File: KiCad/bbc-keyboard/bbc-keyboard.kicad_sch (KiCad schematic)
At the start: 11 parts

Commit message: LEDs
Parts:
- LD1, LD2, LD3: footprint (none) -> LED_THT:LED_D5.0mm
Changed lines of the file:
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@@
       (effects (font (size 1.27 1.27)) (justify right))
     )
-    (property "Footprint" "" (id 2) (at 71.12 73.66 0)
+    (property "Footprint" "LED_THT:LED_D5.0mm" (id 2) (at 71.12 73.66 0)
       (effects (font (size 1.27 1.27)) hide)
     )
@@
       (effects (font (size 1.27 1.27)) (justify right))
     )
-    (property "Footprint" "" (id 2) (at 80.01 73.66 0)
+    (property "Footprint" "LED_THT:LED_D5.0mm" (id 2) (at 80.01 73.66 0)
       (effects (font (size 1.27 1.27)) hide)
     )
@@
       (effects (font (size 1.27 1.27)) (justify right))
     )
-    (property "Footprint" "" (id 2) (at 88.9 73.66 0)
+    (property "Footprint" "LED_THT:LED_D5.0mm" (id 2) (at 88.9 73.66 0)
       (effects (font (size 1.27 1.27)) hide)
     )
@@
     )
     (path "/5414043a-ed38-4cec-828b-be5302069545"
-      (reference "LD1") (unit 1) (value "SHIFT") (footprint "")
+      (reference "LD1") (unit 1) (value "SHIFT") (footprint "LED_THT:LED_D5.0mm")
     )
     (path "/6e00e269-9889-489b-868d-4b59dc264727"
-      (reference "LD2") (unit 1) (value "CAPS") (footprint "")
+      (reference "LD2") (unit 1) (value "CAPS") (footprint "LED_THT:LED_D5.0mm")
     )
     (path "/9c0a84d6-0b56-4721-ac67-8bdfe3f07465"
-      (reference "LD3") (unit 1) (value "CAS") (footprint "")
+      (reference "LD3") (unit 1) (value "CAS") (footprint "LED_THT:LED_D5.0mm")
     )
     (path "/9d392708-6605-40d8-adaf-84e4e23a6904"

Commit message: placing components
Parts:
- C1, C2, C3: footprint (none) -> Capacitor_THT:C_Disc_D9.0mm_W2.5mm_P5.00mm
- C4: footprint (none) -> Capacitor_THT:CP_Radial_D5.0mm_P2.00mm
- PL1: footprint (none) -> Connector_PinHeader_2.54mm:PinHeader_1x17_P2.54mm_Horizontal
- R1, R2, R3: footprint (none) -> Resistor_THT:R_Axial_DIN0309_L9.0mm_D3.2mm_P12.70mm_Horizontal
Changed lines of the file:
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@@
       (effects (font (size 1.27 1.27)) (justify left))
     )
-    (property "Footprint" "" (id 2) (at 238.4552 123.19 0)
+    (property "Footprint" "Capacitor_THT:C_Disc_D9.0mm_W2.5mm_P5.00mm" (id 2) (at 238.4552 123.19 0)
       (effects (font (size 1.27 1.27)) hide)
     )
@@
     (property "Reference" "R3" (id 0) (at 55.88 58.42 90))
     (property "Value" "470" (id 1) (at 59.69 57.15 90))
-    (property "Footprint" "" (id 2) (at 59.69 58.928 90)
+    (property "Footprint" "Resistor_THT:R_Axial_DIN0309_L9.0mm_D3.2mm_P12.70mm_Horizontal" (id 2) (at 59.69 58.928 90)
       (effects (font (size 1.27 1.27)) hide)
     )
@@
       (effects (font (size 1.27 1.27)) (justify left))
     )
-    (property "Footprint" "" (id 2) (at 228.2952 123.19 0)
+    (property "Footprint" "Capacitor_THT:C_Disc_D9.0mm_W2.5mm_P5.00mm" (id 2) (at 228.2952 123.19 0)
       (effects (font (size 1.27 1.27)) hide)
     )
@@
       (effects (font (size 1.27 1.27)) (justify left))
     )
-    (property "Footprint" "" (id 2) (at 248.6152 123.19 0)
+    (property "Footprint" "Capacitor_THT:C_Disc_D9.0mm_W2.5mm_P5.00mm" (id 2) (at 248.6152 123.19 0)
       (effects (font (size 1.27 1.27)) hide)
     )
@@
     (property "Reference" "R1" (id 0) (at 55.88 66.04 90))
     (property "Value" "470" (id 1) (at 59.69 64.77 90))
-    (property "Footprint" "" (id 2) (at 59.69 66.548 90)
+    (property "Footprint" "Resistor_THT:R_Axial_DIN0309_L9.0mm_D3.2mm_P12.70mm_Horizontal" (id 2) (at 59.69 66.548 90)
       (effects (font (size 1.27 1.27)) hide)
     )
@@
     (property "Reference" "R2" (id 0) (at 55.88 68.58 90))
     (property "Value" "470" (id 1) (at 59.69 67.31 90))
-    (property "Footprint" "" (id 2) (at 59.69 69.088 90)
+    (property "Footprint" "Resistor_THT:R_Axial_DIN0309_L9.0mm_D3.2mm_P12.70mm_Horizontal" (id 2) (at 59.69 69.088 90)
       (effects (font (size 1.27 1.27)) hide)
     )
@@
     (property "Reference" "PL1" (id 0) (at 26.67 20.32 0))
     (property "Value" "Conn_01x17" (id 1) (at 26.67 22.86 0))
-    (property "Footprint" "" (id 2) (at 26.67 46.99 0)
+    (property "Footprint" "Connector_PinHeader_2.54mm:PinHeader_1x17_P2.54mm_Horizontal" (id 2) (at 26.67 46.99 0)
       (effects (font (size 1.27 1.27)) hide)
     )
@@
       (effects (font (size 1.27 1.27)) (justify left))
     )
-    (property "Footprint" "" (id 2) (at 216.8652 123.19 0)
+    (property "Footprint" "Capacitor_THT:CP_Radial_D5.0mm_P2.00mm" (id 2) (at 216.8652 123.19 0)
       (effects (font (size 1.27 1.27)) hide)
     )
@@
     )
     (path "/1999562b-3aa3-4942-8f9a-0c18378bf41e"
-      (reference "C1") (unit 1) (value "100n") (footprint "")
+      (reference "C1") (unit 1) (value "100n") (footprint "Capacitor_THT:C_Disc_D9.0mm_W2.5mm_P5.00mm")
     )
     (path "/0a52c5cd-cd67-43d5-8e92-e6d7cd699b9e"
-      (reference "C2") (unit 1) (value "100n") (footprint "")
+      (reference "C2") (unit 1) (value "100n") (footprint "Capacitor_THT:C_Disc_D9.0mm_W2.5mm_P5.00mm")
     )
     (path "/635994cc-e386-437c-82fc-237357a7fc1f"
-      (reference "C3") (unit 1) (value "100n") (footprint "")
+      (reference "C3") (unit 1) (value "100n") (footprint "Capacitor_THT:C_Disc_D9.0mm_W2.5mm_P5.00mm")
     )
     (path "/c682d553-74ba-42d9-8889-c09503e55bbb"
-      (reference "C4") (unit 1) (value "22u") (footprint "")
+      (reference "C4") (unit 1) (value "22u") (footprint "Capacitor_THT:CP_Radial_D5.0mm_P2.00mm")
     )
     (path "/5a6afae0-4df7-4603-b305-1b33d5f2e402/68a28416-7f00-45ff-be2b-fbdcc4139499"
-      (reference "D1") (unit 1) (value "D") (footprint "")
+      (reference "D1") (unit 1) (value "D") (footprint "Diode_THT:D_DO-34_SOD68_P12.70mm_Horizontal")
     )
     (path "/5a6afae0-4df7-4603-b305-1b33d5f2e402/bebc2e67-a928-4b74-8640-0b9a8a676dc5"
-      (reference "D2") (unit 1) (value "D") (footprint "")
+      (reference "D2") (unit 1) (value "D") (footprint "Diode_THT:D_DO-34_SOD68_P12.70mm_Horizontal")
     )
     (path "/5a6afae0-4df7-4603-b305-1b33d5f2e402/5070532a-1ff5-4ac7-83d7-db0cf41aa0a7"
-      (reference "D3") (unit 1) (value "D") (footprint "")
+      (reference "D3") (unit 1) (value "D") (footprint "Diode_THT:D_DO-34_SOD68_P12.70mm_Horizontal")
     )
     (path "/5a6afae0-4df7-4603-b305-1b33d5f2e402/f6586281-8c8f-460c-8022-faa0539d24f4"
-      (reference "D4") (unit 1) (value "D") (footprint "")
+      (reference "D4") (unit 1) (value "D") (footprint "Diode_THT:D_DO-34_SOD68_P12.70mm_Horizontal")
     )
     (path "/5a6afae0-4df7-4603-b305-1b33d5f2e402/16e3d287-2e4c-40c3-94b6-147dd1141066"
-      (reference "D5") (unit 1) (value "D") (footprint "")
+      (reference "D5") (unit 1) (value "D") (footprint "Diode_THT:D_DO-34_SOD68_P12.70mm_Horizontal")
     )
     (path "/5a6afae0-4df7-4603-b305-1b33d5f2e402/c96a6a1d-251a-42bc-b229-de6d2685451d"
-      (reference "D6") (unit 1) (value "D") (footprint "")
+      (reference "D6") (unit 1) (value "D") (footprint "Diode_THT:D_DO-34_SOD68_P12.70mm_Horizontal")
     )
     (path "/5a6afae0-4df7-4603-b305-1b33d5f2e402/4db2fdc9-008d-47a1-aaed-a73ddae3d93b"
-      (reference "D7") (unit 1) (value "D") (footprint "")
+      (reference "D7") (unit 1) (value "D") (footprint "Diode_THT:D_DO-34_SOD68_P12.70mm_Horizontal")
     )
     (path "/5a6afae0-4df7-4603-b305-1b33d5f2e402/c59eff60-8aa6-4cc2-ae38-165eecb9bee1"
-      (reference "D8") (unit 1) (value "D") (footprint "")
+      (reference "D8") (unit 1) (value "D") (footprint "Diode_THT:D_DO-34_SOD68_P12.70mm_Horizontal")
     )
     (path "/5a6afae0-4df7-4603-b305-1b33d5f2e402/72d29650-3584-4417-abb0-b973d06f1e74"
-      (reference "D9") (unit 1) (value "D") (footprint "")
+      (reference "D9") (unit 1) (value "D") (footprint "Diode_THT:D_DO-34_SOD68_P12.70mm_Horizontal")
     )
     (path "/5a6afae0-4df7-4603-b305-1b33d5f2e402/2d9d1e39-49bf-41b3-9a78-906601dd003f"
-      (reference "D10") (unit 1) (value "D") (footprint "")
+      (reference "D10") (unit 1) (value "D") (footprint "Diode_THT:D_DO-34_SOD68_P12.70mm_Horizontal")
     )
     (path "/6149d2d9-e610-4c07-b8fa-fc11a7f5479e/9ec18c21-5abd-48d2-93f1-408c3c8d1a4f"
-      (reference "IC1") (unit 1) (value "74LS161") (footprint "")
+      (reference "IC1") (unit 1) (value "74LS161") (footprint "Package_DIP:DIP-16_W7.62mm")
     )
     (path "/6149d2d9-e610-4c07-b8fa-fc11a7f5479e/d4cc5c9d-4914-4245-a9df-14c5b07c2d57"
-      (reference "IC2") (unit 1) (value "74251") (footprint "")
+      (reference "IC2") (unit 1) (value "74251") (footprint "Package_DIP:DIP-16_W7.62mm")
     )
     (path "/6149d2d9-e610-4c07-b8fa-fc11a7f5479e/90787224-6ca3-4c9c-aa33-b356b1ade5db"
-      (reference "IC3") (unit 1) (value "74145") (footprint "")
+      (reference "IC3") (unit 1) (value "74145") (footprint "Package_DIP:DIP-16_W7.62mm")
     )
     (path "/6149d2d9-e610-4c07-b8fa-fc11a7f5479e/df9495c4-1846-4443-819f-1561eebcdbff"
-      (reference "IC4") (unit 1) (value "74LS30") (footprint "")
+      (reference "IC4") (unit 1) (value "74LS30") (footprint "Package_DIP:DIP-14_W7.62mm")
     )
     (path "/5414043a-ed38-4cec-828b-be5302069545"
@@
     )
     (path "/9d392708-6605-40d8-adaf-84e4e23a6904"
-      (reference "PL1") (unit 1) (value "Conn_01x17") (footprint "")
+      (reference "PL1") (unit 1) (value "Conn_01x17") (footprint "Connector_PinHeader_2.54mm:PinHeader_1x17_P2.54mm_Horizontal")
     )
     (path "/77fd05e2-49e6-4d07-8e13-f9d8c7fba4ff"
-      (reference "R1") (unit 1) (value "470") (footprint "")
+      (reference "R1") (unit 1) (value "470") (footprint "Resistor_THT:R_Axial_DIN0309_L9.0mm_D3.2mm_P12.70mm_Horizontal")
     )
     (path "/807c5fad-ab65-416a-ad00-d87c4516ce11"
-      (reference "R2") (unit 1) (value "470") (footprint "")
+      (reference "R2") (unit 1) (value "470") (footprint "Resistor_THT:R_Axial_DIN0309_L9.0mm_D3.2mm_P12.70mm_Horizontal")
     )
     (path "/130b947a-960e-4937-976b-f934fa3a4c34"
-      (reference "R3") (unit 1) (value "470") (footprint "")
+      (reference "R3") (unit 1) (value "470") (footprint "Resistor_THT:R_Axial_DIN0309_L9.0mm_D3.2mm_P12.70mm_Horizontal")
     )
     (path "/6149d2d9-e610-4c07-b8fa-fc11a7f5479e/5f7393c9-182d-44b2-92db-9c3cee6bcbf1"
@@
     )
     (path "/5a6afae0-4df7-4603-b305-1b33d5f2e402/0239b9d2-1438-472c-beb0-c9700dba7bc0"
-      (reference "SW74") (unit 1) (value "SW_DIP_x08") (footprint "")
+      (reference "SW74") (unit 1) (value "SW_DIP_x08") (footprint "Button_Switch_THT:SW_DIP_SPSTx08_Slide_9.78x22.5mm_W7.62mm_P2.54mm")
     )
     (path "/5a6afae0-4df7-4603-b305-1b33d5f2e402/53f914f1-d751-4149-8cd9-30532b860fe7"

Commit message: DRC pass
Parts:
- PL1: footprint Connector_PinHeader_2.54mm:PinHeader_1x17_P2.54mm_Horizontal -> SpecialConnectors:PinHeader_1x17_P2.54mm_Horizontal_noSilk
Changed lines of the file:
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@@
     (property "Reference" "PL1" (id 0) (at 26.67 20.32 0))
     (property "Value" "Conn_01x17" (id 1) (at 26.67 22.86 0))
-    (property "Footprint" "Connector_PinHeader_2.54mm:PinHeader_1x17_P2.54mm_Horizontal" (id 2) (at 26.67 46.99 0)
+    (property "Footprint" "SpecialConnectors:PinHeader_1x17_P2.54mm_Horizontal_noSilk" (id 2) (at 26.67 46.99 0)
       (effects (font (size 1.27 1.27)) hide)
     )
@@
     )
     (path "/9d392708-6605-40d8-adaf-84e4e23a6904"
-      (reference "PL1") (unit 1) (value "Conn_01x17") (footprint "Connector_PinHeader_2.54mm:PinHeader_1x17_P2.54mm_Horizontal")
+      (reference "PL1") (unit 1) (value "Conn_01x17") (footprint "SpecialConnectors:PinHeader_1x17_P2.54mm_Horizontal_noSilk")
     )
     (path "/77fd05e2-49e6-4d07-8e13-f9d8c7fba4ff"

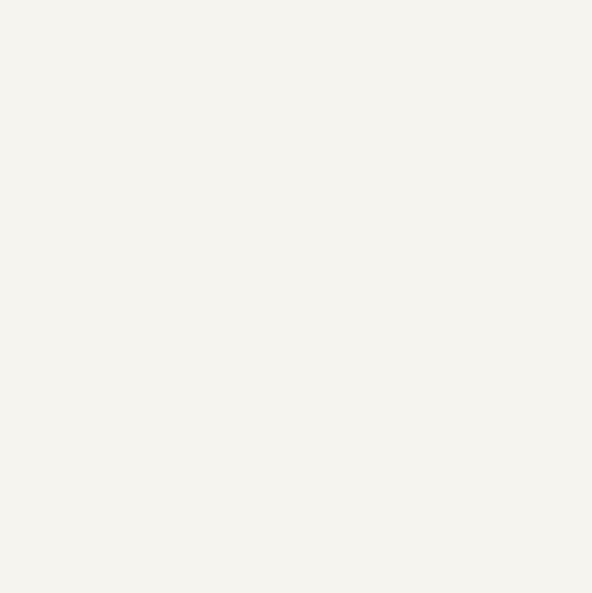
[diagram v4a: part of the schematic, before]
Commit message: mounting holes for backplates
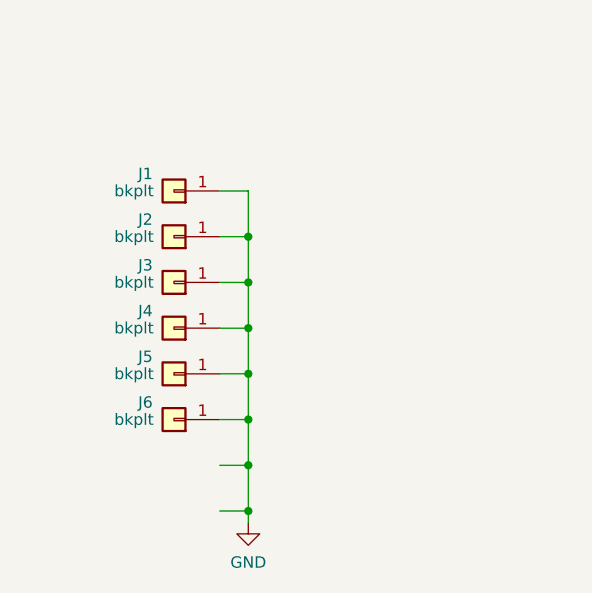
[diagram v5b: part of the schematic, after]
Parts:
- added J1, J2, J3, J4, J5, J6: bkplt, MountingHole:MountingHole_2.7mm_M2.5_DIN965_Pad, symbol Connector_Generic:Conn_01x01
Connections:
- net GND: now also J1.1 (Pin_1), J2.1 (Pin_1), J3.1 (Pin_1), J4.1 (Pin_1), J5.1 (Pin_1), J6.1 (Pin_1)

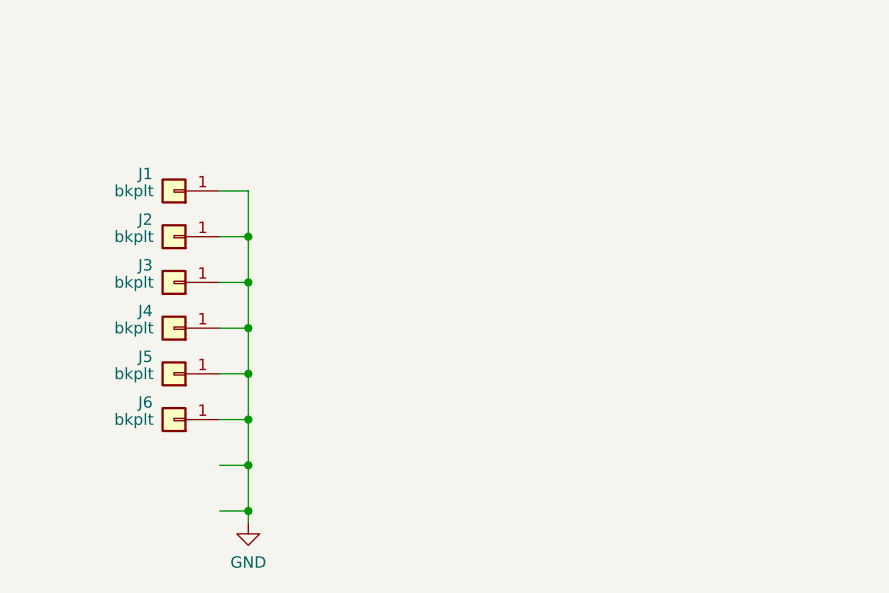
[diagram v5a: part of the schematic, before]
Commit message: mounting holes
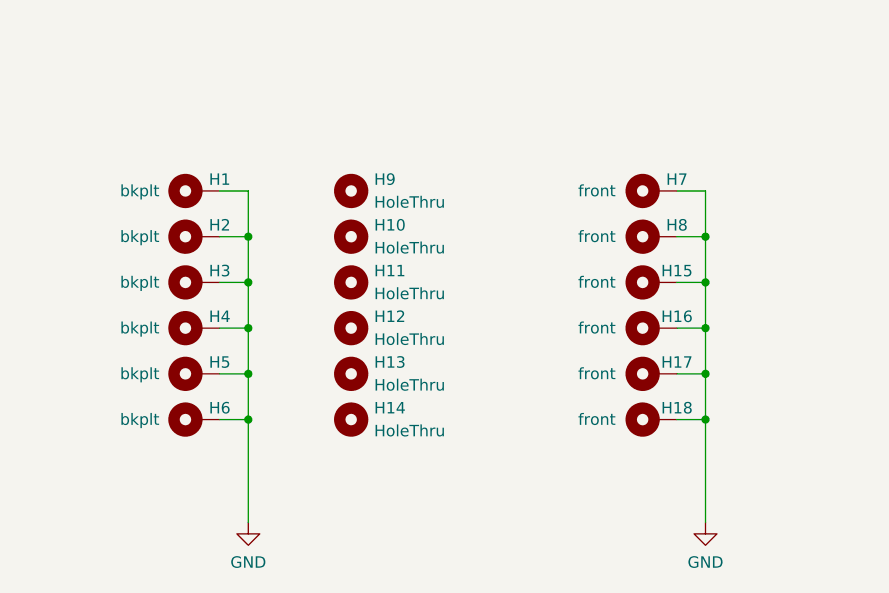
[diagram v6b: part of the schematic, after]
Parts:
- removed J1, J2, J3, J4, J5, J6: bkplt, MountingHole:MountingHole_2.7mm_M2.5_DIN965_Pad, symbol Connector_Generic:Conn_01x01
- added H1, H2, H3, H4, H5, H6: bkplt, MountingHole:MountingHole_2.7mm_M2.5_DIN965_Pad, symbol Mechanical:MountingHole_Pad
- added H10, H11, H12, H13, H14, H9: HoleThru, MountingHole:MountingHole_6.5mm, symbol Mechanical:MountingHole
- added H15, H16, H17, H18, H7, H8: front, MountingHole:MountingHole_2.7mm_M2.5_DIN965_Pad, symbol Mechanical:MountingHole_Pad
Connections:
- net GND: now also H1.1, H15.1, H16.1, H17.1, H18.1, H2.1, H3.1, H4.1, H5.1, H6.1, H7.1, H8.1
